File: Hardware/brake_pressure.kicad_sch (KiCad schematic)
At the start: 13 parts, among them U15 MCP6002-xMS

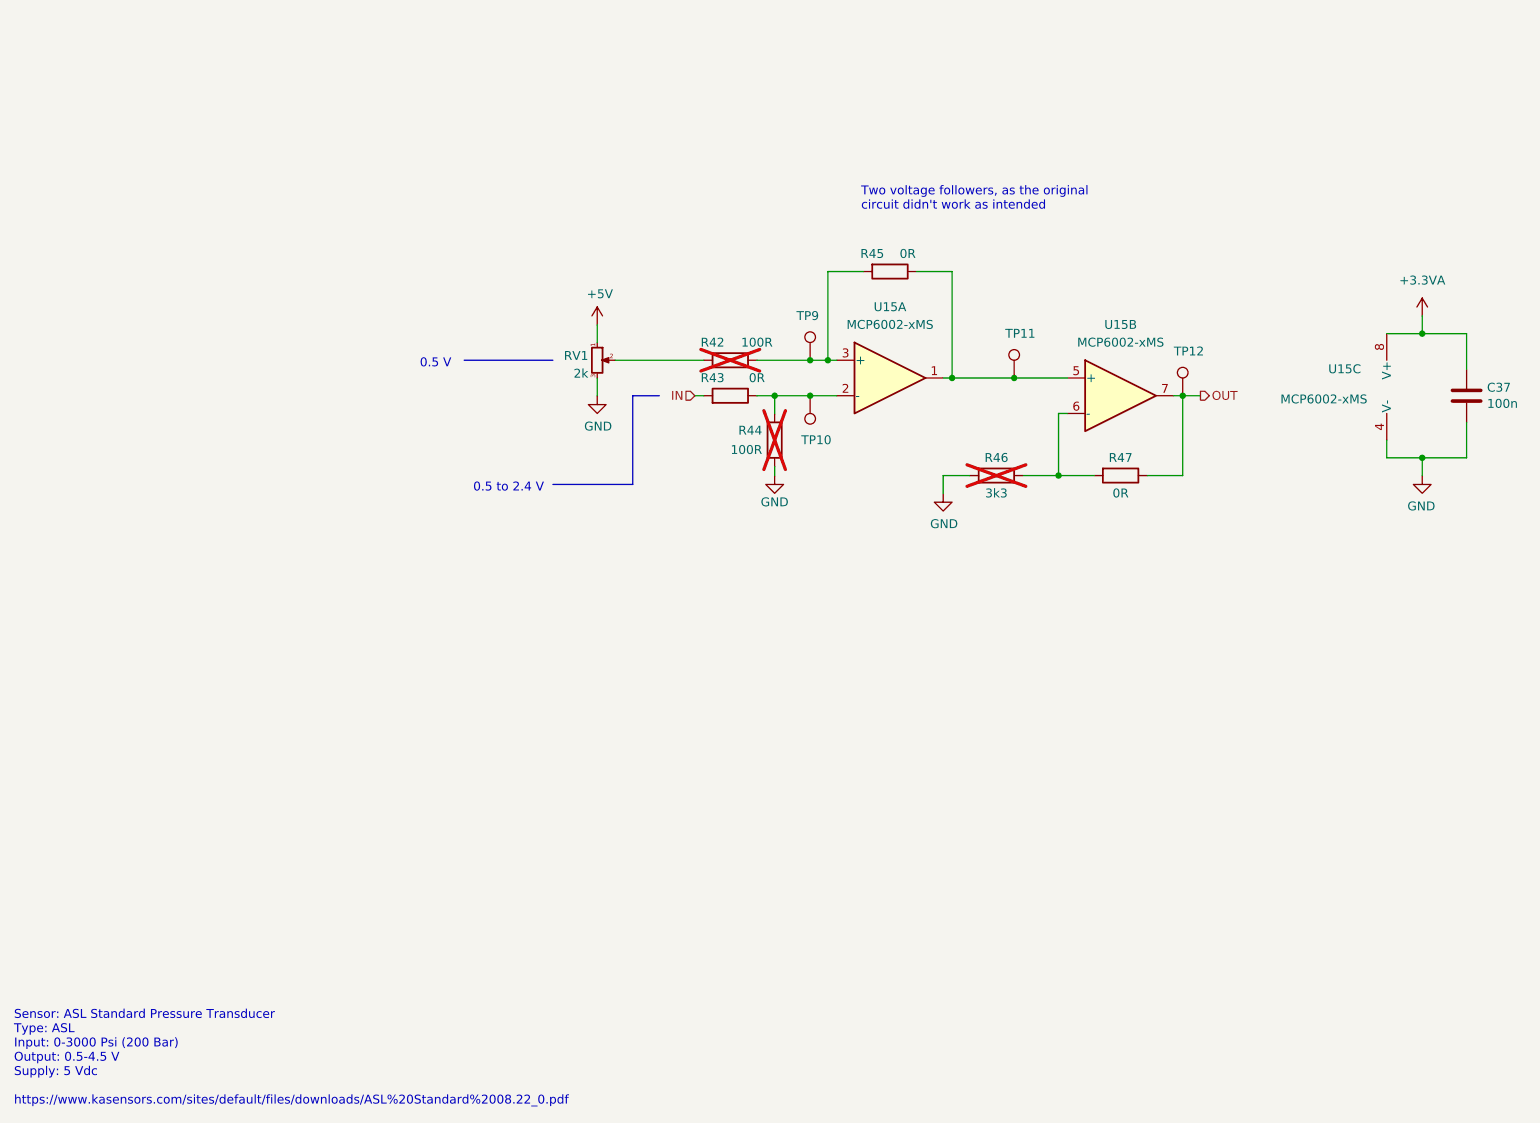
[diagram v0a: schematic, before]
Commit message: Created new hardware version 2.0
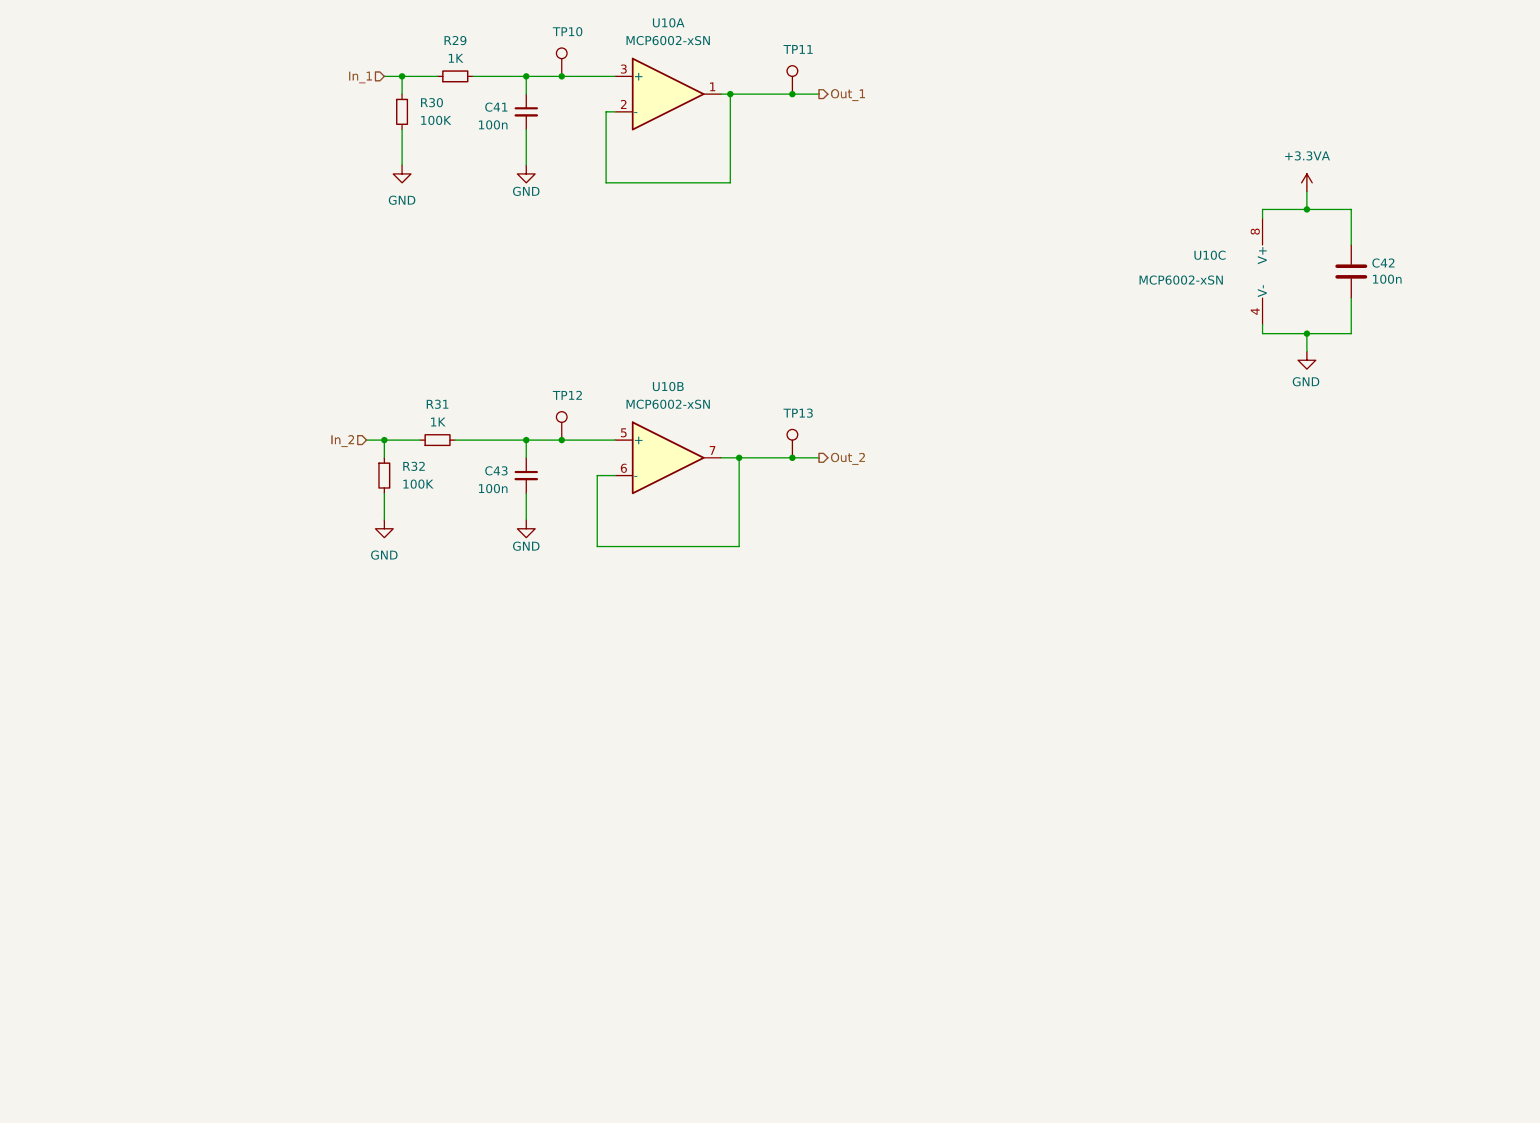
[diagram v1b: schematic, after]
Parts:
- removed R42, R44: 100R, Resistor_SMD:R_0603_1608Metric_Pad0.98x0.95mm_HandSolder, symbol Device:R
- removed R43, R45, R47: 0R, Resistor_SMD:R_0603_1608Metric_Pad0.98x0.95mm_HandSolder, symbol Device:R
- removed R46: 3k3, Resistor_SMD:R_0603_1608Metric_Pad0.98x0.95mm_HandSolder, symbol Device:R
- removed RV1: 2k, Potentiometer_SMD:Potentiometer_Bourns_3214J_Horizontal, symbol Device:R_Potentiometer_Small
- removed TP9: BR_N, TestPoint:TestPoint_THTPad_D1.0mm_Drill0.5mm, symbol Connector:TestPoint
- removed U15: MCP6002-xMS, Snapeda:SOP65P490X110-8N, symbol Amplifier_Operational:MCP6002-xMS
- added C41, C43: 100n, Capacitor_SMD:C_0603_1608Metric_Pad1.08x0.95mm_HandSolder, symbol Device:C_Small
- added R29, R31: 1K, Resistor_SMD:R_0603_1608Metric_Pad0.98x0.95mm_HandSolder, symbol Device:R_Small
- added R30, R32: 100K, Resistor_SMD:R_0603_1608Metric_Pad0.98x0.95mm_HandSolder, symbol Device:R_Small
- added TP13: APPS_MID, TestPoint:TestPoint_THTPad_D1.0mm_Drill0.5mm, symbol Connector:TestPoint
- added U10: MCP6002-xSN, Package_SO:SOIC-8_3.9x4.9mm_P1.27mm, symbol Amplifier_Operational:MCP6002-xSN
- TP10: value BR_P -> APPS_MID
- TP11: value BR_MID -> APPS_MID
- TP12: value BR_OUT -> APPS_MID
- renumbered C37 to C42
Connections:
- net +3.3VA: now also U10.8 (V+)
- net GND: now also C41.2, C43.2, R30.2, R32.2, U10.4 (V-)
- net Out_1: now reaches TP11.1
- net Out_1: now also U10.1, U10.2 (-)
- net at TP10.1: now also C41.1, R29.2, U10.3 (+)
- net OUT: no longer names the net of TP12.1
- net OUT: now also C43.1, R31.2, U10.5 (+)
- new net In_1: R29.1, R30.1
- new net In_2: R31.1, R32.1
- new net Out_2: TP13.1, U10.6 (-), U10.7
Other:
- note removed: "0.5 V"
- note removed: "0.5 to 2.4 V"
- company: Author: Szymon Kostrubiec -> (none)
- title: Brake pressure -> (none)
- moved on the sheet: C42

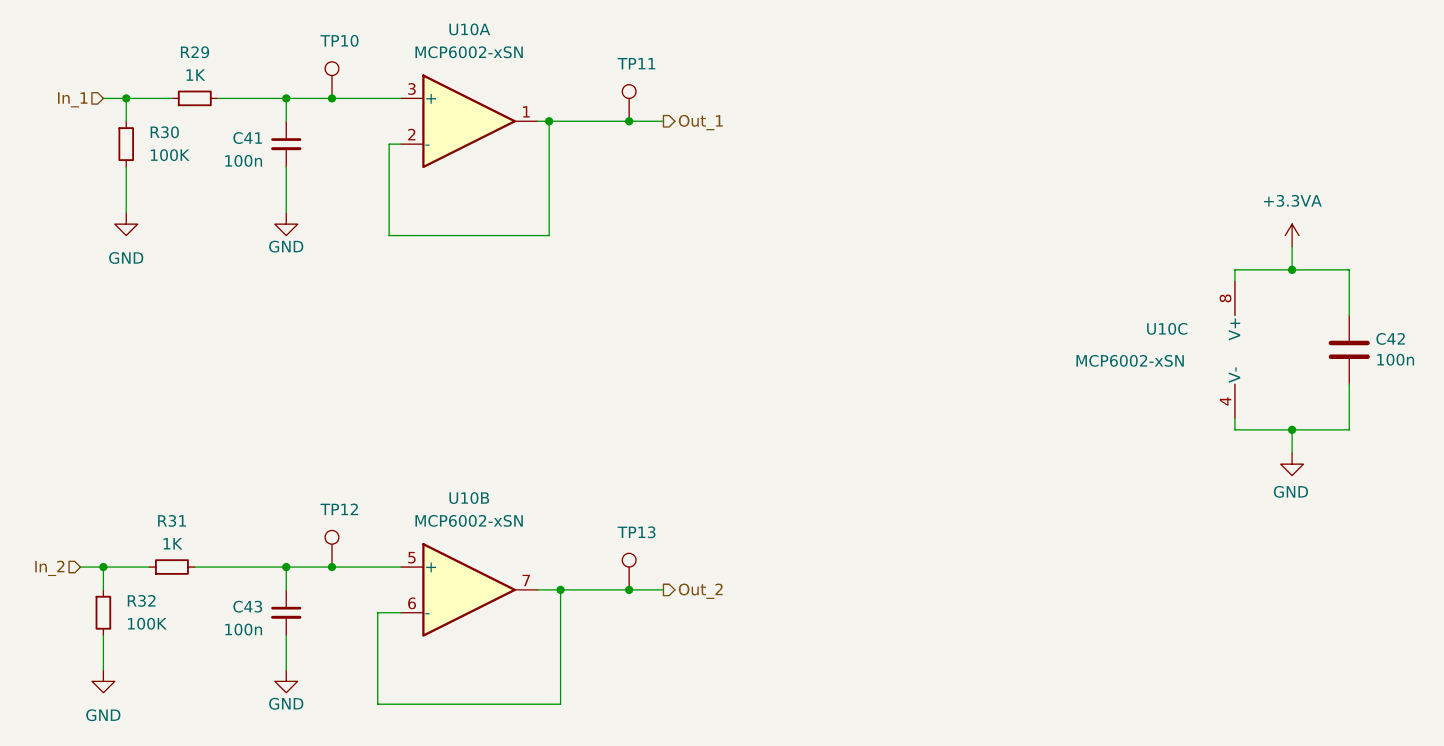
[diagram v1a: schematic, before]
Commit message: Changes in schematic, separated CAN buses, added XIAO Sense S3 DevBoard
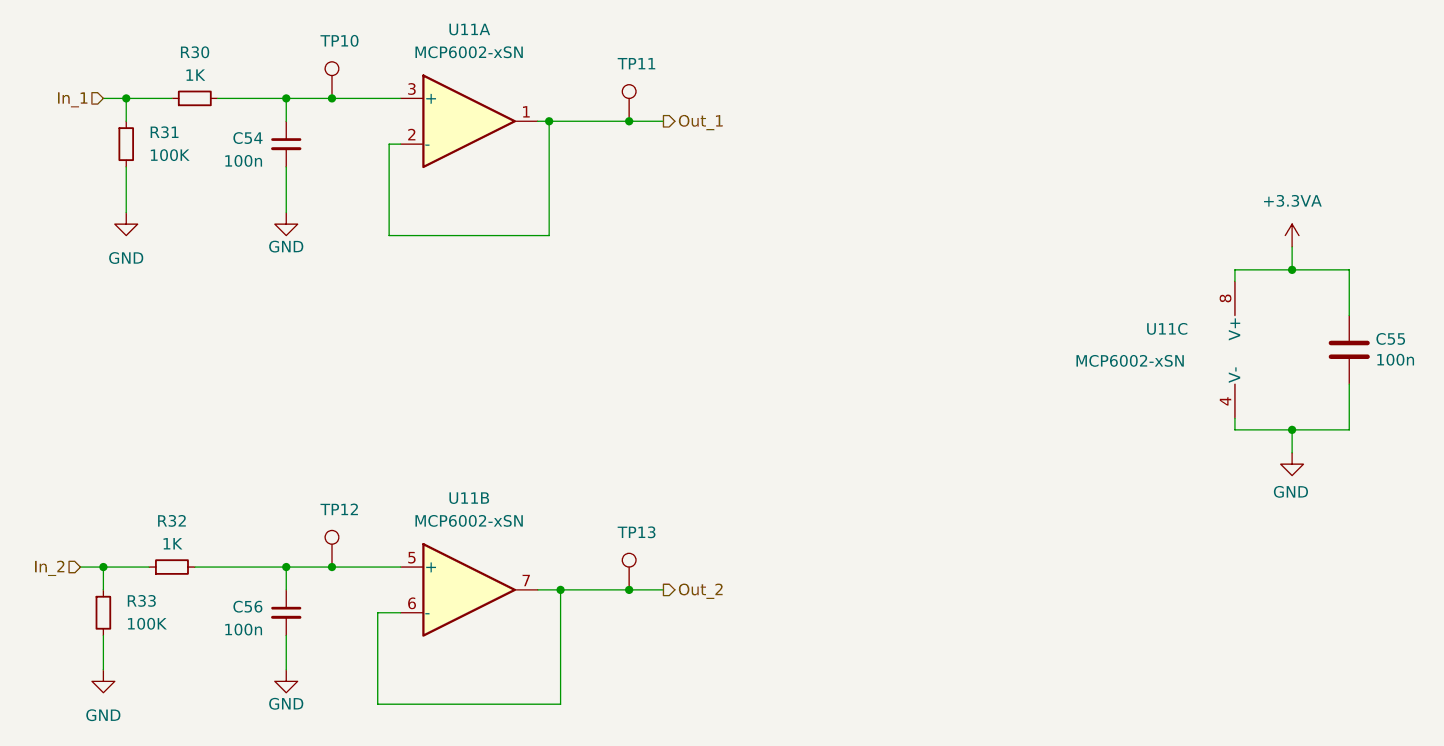
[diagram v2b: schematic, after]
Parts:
- renumbered C41 to C54, C42 to C55, C43 to C56, R29 to R30, R30 to R31, R31 to R32, R32 to R33, U10 to U11
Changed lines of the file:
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@@
 		(on_board yes)
 		(dnp no)
-		(property "Reference" "C41"
+		(property "Reference" "C54"
 			(at 83.82 55.2513 0)
 			(effects
@@
 			(project "PUTM_EV_Frontbox"
 				(path "/b652b05a-4e3d-4ad1-b032-18886abe7d45/678f2262-c7cf-4abf-8896-ac0160b6b5fa"
-					(reference "C41")
+					(reference "C54")
 					(unit 1)
 				)
@@
 		(dnp no)
 		(fields_autoplaced yes)
-		(property "Reference" "R32"
+		(property "Reference" "R33"
 			(at 68.58 106.6799 0)
 			(effects
@@
 			(project "PUTM_EV_Frontbox"
 				(path "/b652b05a-4e3d-4ad1-b032-18886abe7d45/678f2262-c7cf-4abf-8896-ac0160b6b5fa"
-					(reference "R32")
+					(reference "R33")
 					(unit 1)
 				)
@@
 		(dnp no)
 		(fields_autoplaced yes)
-		(property "Reference" "R30"
+		(property "Reference" "R31"
 			(at 71.12 54.6099 0)
 			(effects
@@
 			(project "PUTM_EV_Frontbox"
 				(path "/b652b05a-4e3d-4ad1-b032-18886abe7d45/678f2262-c7cf-4abf-8896-ac0160b6b5fa"
-					(reference "R30")
+					(reference "R31")
 					(unit 1)
 				)
@@
 		(on_board yes)
 		(dnp no)
-		(property "Reference" "#PWR083"
+		(property "Reference" "#PWR089"
 			(at 86.36 69.85 0)
 			(effects
@@
 			(project "PUTM_EV_Frontbox"
 				(path "/b652b05a-4e3d-4ad1-b032-18886abe7d45/678f2262-c7cf-4abf-8896-ac0160b6b5fa"
-					(reference "#PWR083")
+					(reference "#PWR089")
 					(unit 1)
 				)
@@
 		(dnp no)
 		(fields_autoplaced yes)
-		(property "Reference" "#PWR082"
+		(property "Reference" "#PWR088"
 			(at 68.58 69.85 0)
 			(effects
@@
 			(project "PUTM_EV_Frontbox"
 				(path "/b652b05a-4e3d-4ad1-b032-18886abe7d45/678f2262-c7cf-4abf-8896-ac0160b6b5fa"
-					(reference "#PWR082")
+					(reference "#PWR088")
 					(unit 1)
 				)
@@
 		(on_board yes)
 		(dnp no)
-		(property "Reference" "#PWR085"
+		(property "Reference" "#PWR091"
 			(at 198.12 96.52 0)
 			(effects
@@
 			(project "PUTM_EV_Frontbox"
 				(path "/b652b05a-4e3d-4ad1-b032-18886abe7d45/678f2262-c7cf-4abf-8896-ac0160b6b5fa"
-					(reference "#PWR085")
+					(reference "#PWR091")
 					(unit 1)
 				)
@@
 		(on_board yes)
 		(dnp no)
-		(property "Reference" "C43"
+		(property "Reference" "C56"
 			(at 83.82 107.3213 0)
 			(effects
@@
 			(project "PUTM_EV_Frontbox"
 				(path "/b652b05a-4e3d-4ad1-b032-18886abe7d45/678f2262-c7cf-4abf-8896-ac0160b6b5fa"
-					(reference "C43")
+					(reference "C56")
 					(unit 1)
 				)
@@
 		(dnp no)
 		(fields_autoplaced yes)
-		(property "Reference" "#PWR086"
+		(property "Reference" "#PWR092"
 			(at 66.04 120.65 0)
 			(effects
@@
 			(project "PUTM_EV_Frontbox"
 				(path "/b652b05a-4e3d-4ad1-b032-18886abe7d45/678f2262-c7cf-4abf-8896-ac0160b6b5fa"
-					(reference "#PWR086")
+					(reference "#PWR092")
 					(unit 1)
 				)
@@
 		(dnp no)
 		(fields_autoplaced yes)
-		(property "Reference" "U10"
+		(property "Reference" "U11"
 			(at 106.68 95.25 0)
 			(effects
@@
 			(project ""
 				(path "/b652b05a-4e3d-4ad1-b032-18886abe7d45/678f2262-c7cf-4abf-8896-ac0160b6b5fa"
-					(reference "U10")
+					(reference "U11")
 					(unit 2)
 				)
@@
 		(on_board yes)
 		(dnp no)
-		(property "Reference" "#PWR084"
+		(property "Reference" "#PWR090"
 			(at 198.12 71.12 0)
 			(effects
@@
 			(project "PUTM_EV_Frontbox"
 				(path "/b652b05a-4e3d-4ad1-b032-18886abe7d45/678f2262-c7cf-4abf-8896-ac0160b6b5fa"
-					(reference "#PWR084")
+					(reference "#PWR090")
 					(unit 1)
 				)
@@
 		(dnp no)
 		(fields_autoplaced yes)
-		(property "Reference" "U10"
+		(property "Reference" "U11"
 			(at 106.68 43.18 0)
 			(effects
@@
 			(project ""
 				(path "/b652b05a-4e3d-4ad1-b032-18886abe7d45/678f2262-c7cf-4abf-8896-ac0160b6b5fa"
-					(reference "U10")
+					(reference "U11")
 					(unit 1)
 				)
@@
 		(on_board yes)
 		(dnp no)
-		(property "Reference" "C42"
+		(property "Reference" "C55"
 			(at 207.391 77.5716 0)
 			(effects
@@
 			(project "PUTM_EV_Frontbox"
 				(path "/b652b05a-4e3d-4ad1-b032-18886abe7d45/678f2262-c7cf-4abf-8896-ac0160b6b5fa"
-					(reference "C42")
+					(reference "C55")
 					(unit 1)
 				)
@@
 		(on_board yes)
 		(dnp no)
-		(property "Reference" "U10"
+		(property "Reference" "U11"
 			(at 181.864 76.454 0)
 			(effects
@@
 			(project ""
 				(path "/b652b05a-4e3d-4ad1-b032-18886abe7d45/678f2262-c7cf-4abf-8896-ac0160b6b5fa"
-					(reference "U10")
+					(reference "U11")
 					(unit 3)
 				)
@@
 		(dnp no)
 		(fields_autoplaced yes)
-		(property "Reference" "R29"
+		(property "Reference" "R30"
 			(at 76.2 45.72 90)
 			(effects
@@
 			(project "PUTM_EV_Frontbox"
 				(path "/b652b05a-4e3d-4ad1-b032-18886abe7d45/678f2262-c7cf-4abf-8896-ac0160b6b5fa"
-					(reference "R29")
+					(reference "R30")
 					(unit 1)
 				)
@@
 		(on_board yes)
 		(dnp no)
-		(property "Reference" "#PWR087"
+		(property "Reference" "#PWR093"
 			(at 86.36 120.65 0)
 			(effects
@@
 			(project "PUTM_EV_Frontbox"
 				(path "/b652b05a-4e3d-4ad1-b032-18886abe7d45/678f2262-c7cf-4abf-8896-ac0160b6b5fa"
-					(reference "#PWR087")
+					(reference "#PWR093")
 					(unit 1)
 				)
@@
 		(dnp no)
 		(fields_autoplaced yes)
-		(property "Reference" "R31"
+		(property "Reference" "R32"
 			(at 73.66 97.79 90)
 			(effects
@@
 			(project "PUTM_EV_Frontbox"
 				(path "/b652b05a-4e3d-4ad1-b032-18886abe7d45/678f2262-c7cf-4abf-8896-ac0160b6b5fa"
-					(reference "R31")
-					(unit 1)
-				)
+					(reference "R32")
+					(unit 1)
+				)

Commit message: Initial layout, changes in safety sensing bus labels
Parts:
- TP11, TP13: value APPS_MID -> BRAKE_OUT
- TP12: value APPS_MID -> BRAKE_MID
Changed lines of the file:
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@@
 			)
 		)
-		(property "Value" "APPS_MID"
+		(property "Value" "BRAKE_OUT"
 			(at 127 51.943 0)
 			(effects
@@
 			)
 		)
-		(property "Value" "APPS_MID"
+		(property "Value" "BRAKE_OUT"
 			(at 127 104.013 0)
 			(effects
@@
 			)
 		)
-		(property "Value" "APPS_MID"
+		(property "Value" "BRAKE_MID"
 			(at 93.98 101.473 0)
 			(effects

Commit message: Changes in CAN section
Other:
- title: (none) -> FrontBox
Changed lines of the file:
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@@
 	(generator_version "9.0")
 	(paper "A4")
+	(title_block
+		(title "FrontBox")
+	)
 	(junction
 		(at 91.44 50.8)

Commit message: BOM update
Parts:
- C54, C55, C56, R30, R31, R32, R33: Mouser Part Number (none) -> .
- U11: Mouser Part Number (none) -> 579-MCP6002-E/SN
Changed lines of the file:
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@@
+			)
+		)
+		(property "Mouser Part Number" "."
+			(at 86.36 55.88 0)
+			(effects
+				(font
+					(size 1.27 1.27)
+				)
 			)
 		)
@@
 			)
 		)
+		(property "Mouser Part Number" "."
+			(at 66.04 107.95 0)
+			(effects
+				(font
+					(size 1.27 1.27)
+				)
+			)
+		)
 		(pin "2"
 		)
@@
 			)
 		)
+		(property "Mouser Part Number" "."
+			(at 68.58 55.88 0)
+			(effects
+				(font
+					(size 1.27 1.27)
+				)
+			)
+		)
 		(pin "2"
 		)
@@
 			)
 		)
+		(property "Mouser Part Number" "."
+			(at 86.36 107.95 0)
+			(effects
+				(font
+					(size 1.27 1.27)
+				)
+			)
+		)
 		(pin "1"
 		)
@@
 			)
 		)
+		(property "Mouser Part Number" "579-MCP6002-E/SN"
+			(at 106.68 105.41 0)
+			(effects
+				(font
+					(size 1.27 1.27)
+				)
+				(hide yes)
+			)
+		)
 		(pin "2"
 		)
@@
 			)
 		)
+		(property "Mouser Part Number" "579-MCP6002-E/SN"
+			(at 106.68 53.34 0)
+			(effects
+				(font
+					(size 1.27 1.27)
+				)
+				(hide yes)
+			)
+		)
 		(pin "2"
 		)
@@
 				)
 				(hide yes)
+			)
+		)
+		(property "Mouser Part Number" "."
+			(at 204.47 78.74 0)
+			(effects
+				(font
+					(size 1.27 1.27)
+				)
 			)
 		)
@@
 			)
 		)
+		(property "Mouser Part Number" "579-MCP6002-E/SN"
+			(at 194.31 78.74 0)
+			(effects
+				(font
+					(size 1.27 1.27)
+				)
+				(hide yes)
+			)
+		)
 		(pin "2"
 		)
@@
 			)
 		)
+		(property "Mouser Part Number" "."
+			(at 76.2 50.8 0)
+			(effects
+				(font
+					(size 1.27 1.27)
+				)
+			)
+		)
 		(pin "2"
 		)
@@
 			)
 		)
+		(property "Mouser Part Number" "."
+			(at 73.66 102.87 0)
+			(effects
+				(font
+					(size 1.27 1.27)
+				)
+			)
+		)
